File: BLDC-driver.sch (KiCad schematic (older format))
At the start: 109 parts, among them J1 PROG/DBG, J2 DBG, J3 RS485, J4 Encoder, J5 Conn_01x06, Q1 FDMS8018, Q2 FDMS8018, Q3 FDMS8018, Q4 FDMS8018, Q5 FDMS8018, Q6 FDMS8018, Q7 BC807, U1 NCP81155, U11 SN75176AD, U2 STM32L412CB, U4 NCP81155, U5 NCP81155, U6 MP2359, U7 MIC5504-3.3YM5, U8 NCS213RSQT2G, U9 NCS213RSQT2G, Y1 16MHz

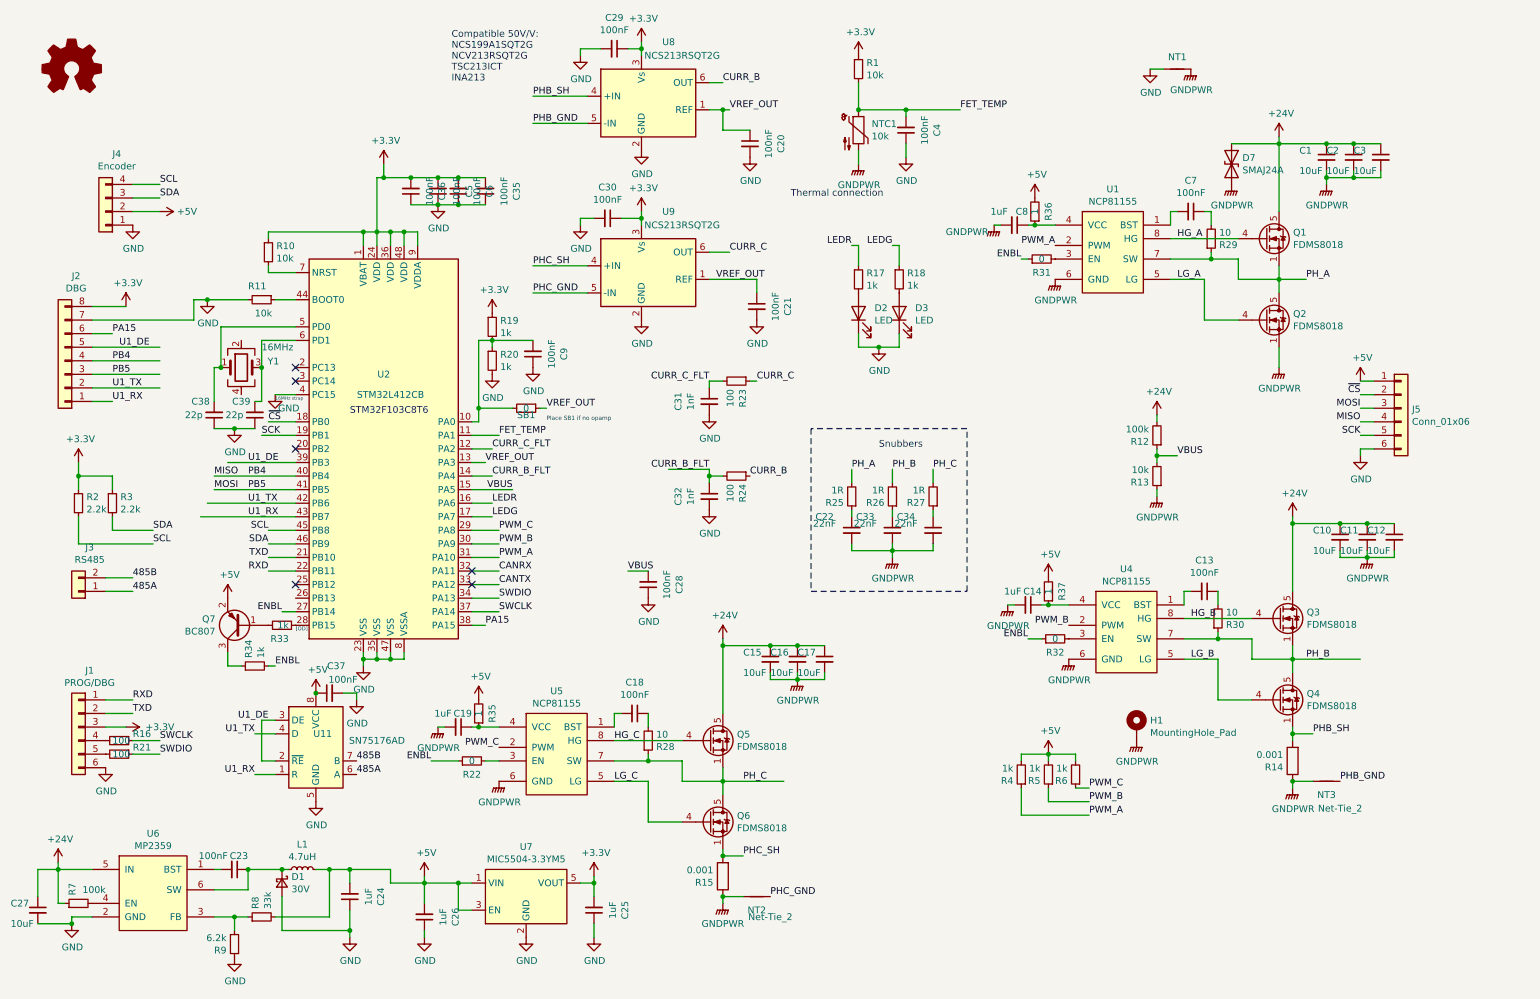
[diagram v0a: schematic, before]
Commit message: Update JLC BOM
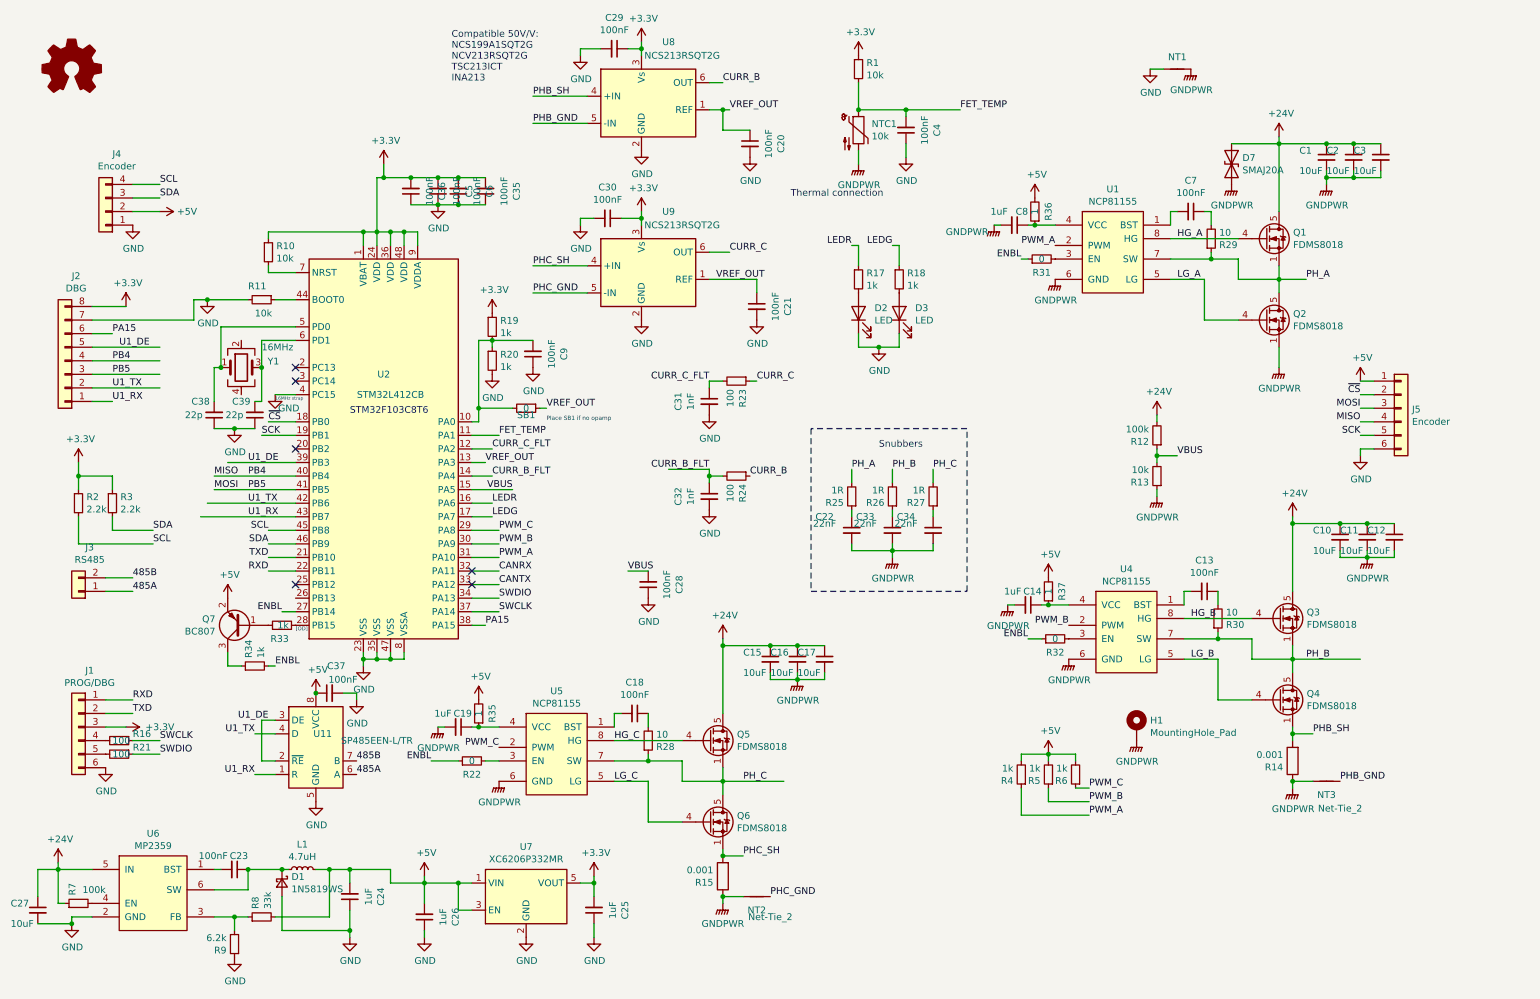
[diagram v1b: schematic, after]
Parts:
- C13, C18, C20, C21, C23, C28, C29, C30, C35, C36, C37, C4, C5, C6, C7, C9: Description [Basic] 100nF ±10% 16V X7R 0402 Multilayer Ceramic Capacito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 -> [Basic] X7R 100nF ±10% 16V 0402 Multilayer Ceramic Capacito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
- D1: value 30V -> 1N5819WS; Description (none) -> [Basic] 40V 1A 600mV @ 1A SOD-323 Schottky Barrier Diodes (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; JLCSMT (none) -> C191023; JLCSMT_PKG (none) -> SOD-323; MFR (none) -> Guangdong Hottech; MPN (none) -> 1N5819WS
- D2: Description LED, RED, 0603 -> [Basic] Red 615~630nm 1.9~2.2V 0603 Light Emitting Diodes (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; JLCSMT_PKG 0603 -> LED_0603
- D7: value SMAJ24A -> SMAJ20A; Description [Extended] Unidirectional 24V 26.7V 38.9V 10.3A SMA(DO-214A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 -> [Extended] Unidirectional 12.3A 32.4V 22.2V 20V SMA TVS ROHS; JLCSMT C10769 -> C353466; JLCSMT_PKG SMA,DO-214AC -> SMA; MFR RUILON(Shenzhen Ruilongyuan Elec) -> Shandong Jingdao Microelectronics; MPN SMAJ24A -> SMAJ20A
- J5: value Conn_01x06 -> Encoder; Description (none) -> [Extended] 6 0.020\"（0.50mm） 0.039\"（1.00mm） Forward Slip C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; JLCSMT_PKG (none) -> FPC-SMD; MFR (none) -> XFCN; MPN (none) -> F0502-B-06-10G-R
- R14, R15: Description [Extended] 0.001Ω ±1% 1W ±75ppm/℃ 1206 Current Sense Resist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 -> [Extended] ±75ppm/℃ ±1% 1W 0.001Ω 1206 Current Sense Resist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
- U1, U4, U5: Description (none) -> [Extended] DFN-8 Gate Drive ICs ROHS; JLCSMT (none) -> C173765; JLCSMT_PKG (none) -> DFN-8_EP_3.0x3.0x0.5P; MFR (none) -> ON Semiconductor; MPN NCP81151MNTBG -> NCP81155MNTXG
- U11: value SN75176AD -> SP485EEN-L/TR; Description [Basic] Transceiver RS485 1/1 SOIC-8_150mil RS-485/RS-422 I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 -> [Basic] Transceiver 1/1 RS485 10Mbps SOIC-8_150mil RS-485/R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; JLCSMT C7063 -> C6855; MFR Texas Instruments -> MaxLinear; MPN SN75176BDR -> SP485EEN-L/TR
- U2: Description (none) -> [Extended] 2.6V ~ 3.6V 32-Bit ARM? Cortex?-M3 108MHz FLASH 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; JLCSMT (none) -> C77994; JLCSMT_PKG (none) -> TQFP-48_7.0x7.0x0.5P; MFR (none) -> GigaDevice Semicon Beijing; MPN (none) -> GD32F103C8T6
- U7: value MIC5504-3.3YM5 -> XC6206P332MR; Description (none) -> [Basic] Low Dropout Regulators(LDO) Positive Fixed 680mV @ 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; JLCSMT (none) -> C5446; JLCSMT_PKG (none) -> SOT-23-3L; MFR (none) -> Torex Semicon; MPN (none) -> XC6206P332MR
- U8, U9: Description (none) -> [Extended] SC-70-6(SOT-363) Current-Sensing Amplifiers ROHS; JLCSMT (none) -> C129948; JLCSMT_PKG (none) -> SOT-363; MFR (none) -> Texas Instruments; MPN (none) -> INA213AIDCKT

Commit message: Update 3V3 LDO
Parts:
- U7: footprint Package_TO_SOT_SMD:SOT-23-5 -> Package_TO_SOT_SMD:SOT-23; symbol Regulator_Linear:MIC5504-3.3YM5 -> Regulator_Linear:XC6206PxxxMR
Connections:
- wire segments 337 -> 334
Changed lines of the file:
@@
 L power:GND #PWR046
 U 1 1 5EEF16F9
-P 4250 7350
-F 0 "#PWR046" H 4250 7100 50  0001 C CNN
-F 1 "GND" H 4255 7177 50  0000 C CNN
-F 2 "" H 4250 7350 50  0001 C CNN
-F 3 "" H 4250 7350 50  0001 C CNN
-	1    4250 7350
+P 4200 7250
+F 0 "#PWR046" H 4200 7000 50  0001 C CNN
+F 1 "GND" H 4205 7077 50  0000 C CNN
+F 2 "" H 4200 7250 50  0001 C CNN
+F 3 "" H 4200 7250 50  0001 C CNN
+	1    4200 7250
 	1    0    0    -1
 $EndComp
@@
 $EndComp
 $Comp
-L Regulator_Linear:MIC5504-3.3YM5 U7
+L Regulator_Linear:XC6206PxxxMR U7
 U 1 1 5EEEC834
-P 4250 7050
-F 0 "U7" H 4250 7417 50  0000 C CNN
-F 1 "XC6206P332MR" H 4250 7326 50  0000 C CNN
-F 2 "Package_TO_SOT_SMD:SOT-23-5" H 4250 6650 50  0001 C CNN
-F 3 "https://datasheet.lcsc.com/szlcsc/Torex-Semicon-XC6206P332MR_C5446.pdf" H 4000 7300 50  0001 C CNN
-F 4 "C5446" H 0   0   50  0001 C CNN "JLCSMT"
-F 5 "[Basic] Low Dropout Regulators(LDO) Positive Fixed 680mV @ 100mA 6V 3.3V 200mA SOT-23-3L RoHS" H 0   0   50  0001 C CNN "Description"
-F 6 "XC6206P332MR" H 0   0   50  0001 C CNN "MPN"
-F 7 "Torex Semicon" H 0   0   50  0001 C CNN "MFR"
-F 8 "SOT-23-3L" H 0   0   50  0001 C CNN "JLCSMT_PKG"
-	1    4250 7050
+P 4200 6950
+F 0 "U7" H 4200 7317 50  0000 C CNN
+F 1 "XC6206P332MR" H 4200 7226 50  0000 C CNN
+F 2 "Package_TO_SOT_SMD:SOT-23" H 4200 6550 50  0001 C CNN
+F 3 "https://datasheet.lcsc.com/szlcsc/Torex-Semicon-XC6206P332MR_C5446.pdf" H 3950 7200 50  0001 C CNN
+F 4 "C5446" H -50 -100 50  0001 C CNN "JLCSMT"
+F 5 "[Basic] Low Dropout Regulators(LDO) Positive Fixed 680mV @ 100mA 6V 3.3V 200mA SOT-23-3L RoHS" H -50 -100 50  0001 C CNN "Description"
+F 6 "XC6206P332MR" H -50 -100 50  0001 C CNN "MPN"
+F 7 "Torex Semicon" H -50 -100 50  0001 C CNN "MFR"
+F 8 "SOT-23-3L" H -50 -100 50  0001 C CNN "JLCSMT_PKG"
+	1    4200 6950
 	1    0    0    -1
 $EndComp
@@
 	1550 2000 1350 2000
 Wire Wire Line
-	3850 7150 3750 7150
-Wire Wire Line
-	3750 7150 3750 6950
-Wire Wire Line
-	3750 6950 3850 6950
-Wire Wire Line
 	3500 6900 3500 6950
 Wire Wire Line
-	3500 6950 3750 6950
-Wire Wire Line
 	3500 7100 3500 6950
 Wire Wire Line
 	3500 7350 3500 7300
 Wire Wire Line
-	4650 6950 4750 6950
-Wire Wire Line
 	4750 6950 4750 7050
 Wire Wire Line
@@
 Connection ~ 950  3950
 Connection ~ 6700 1250
-Connection ~ 3750 6950
 Connection ~ 3500 6950
 Connection ~ 4750 6950
@@
 	1    0    0    -1
 $EndComp
+Wire Wire Line
+	3500 6950 3900 6950
+Wire Wire Line
+	4500 6950 4750 6950
 $EndSCHEMATC

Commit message: Add DC-DC compatible notes
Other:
- note added: "Compatible:\nEUP3458\nME3116"
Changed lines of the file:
@@
 Wire Wire Line
 	4500 6950 4750 6950
+Text Notes 1250 7550 0    50   ~ 0
+Compatible:\nEUP3458\nME3116
 $EndSCHEMATC

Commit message: Add another alt
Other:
- note added: "Compatible:\nEUP3458\nME3116\nSSP9451"
- note removed: "Compatible:\nEUP3458\nME3116"
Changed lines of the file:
@@
 Wire Wire Line
 	4500 6950 4750 6950
-Text Notes 1250 7550 0    50   ~ 0
-Compatible:\nEUP3458\nME3116
+Text Notes 1250 7650 0    50   ~ 0
+Compatible:\nEUP3458\nME3116\nSSP9451
 $EndSCHEMATC

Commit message: Rev 4 update
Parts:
- added C40: 100uF, Capacitor_SMD:CP_Elec_8x6.5, symbol Device:CP_Small
- added J6: PWR, Connector_JST:JST_VH_B2PS-VH_1x02_P3.96mm_Horizontal, symbol Connector_Generic:Conn_01x02
- C1, C10, C11, C12, C15, C16, C17, C2, C27, C3: value 10uF -> 22uF; Description [Basic] 10uF ±10% 50V X5R 1206 Multilayer Ceramic Capacitor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 -> [Basic] 25V 22uF X5R ±10% 1206 Multilayer Ceramic Capacitor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; JLCSMT C13585 -> C12891; MPN CL31A106KBHNNNE -> CL31A226KAHNNNE
- C13, C18, C20, C21, C23, C28, C29, C30, C35, C36, C37, C4, C5, C6, C7, C9: Description [Basic] X7R 100nF ±10% 16V 0402 Multilayer Ceramic Capacito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 -> [Basic] 16V 100nF X7R ±10% 0402 Multilayer Ceramic Capacito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
- C14, C19, C24, C8: Description [Basic] 1uF ±10% 25V X5R 0402 Multilayer Ceramic Capacitors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 -> [Basic] 25V 1uF X5R ±10% 0402 Multilayer Ceramic Capacitors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
- C22, C33, C34: Description [Basic] Multilayer Ceramic Capacitors MLCC - SMD/SMT 22nF 5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 -> [Basic] 50V 22nF X7R ±10% 0402 Multilayer Ceramic Capacitor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; MFR Guangdong Fenghua Advanced Tech -> FH(Guangdong Fenghua Advanced Tech)
- C25, C26: Description [Basic] 1uF ±10% 50V X5R 0603 Multilayer Ceramic Capacitors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 -> [Basic] 50V 1uF X5R ±10% 0603 Multilayer Ceramic Capacitors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
- C31, C32: Description [Basic] 1nF ±10% 50V X7R 0402 Multilayer Ceramic Capacitors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 -> [Basic] 50V 1nF X7R ±10% 0402 Multilayer Ceramic Capacitors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
- C38, C39: Description [Basic] 22pF ±5% 50V C0G 0402 Multilayer Ceramic Capacitors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 -> [Basic] 50V 22pF C0G ±5% 0402 Multilayer Ceramic Capacitors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
- D1: Description [Basic] 40V 1A 600mV @ 1A SOD-323 Schottky Barrier Diodes (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 -> [Basic] 40V 600mV@1A 1A SOD-323 Schottky Barrier Diodes (SB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
- D2: Description [Basic] Red 615~630nm 1.9~2.2V 0603 Light Emitting Diodes (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 -> [Basic] 20mA 285mcd 3.3V 518nm Colorless transparence -40℃~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; JLCSMT C2286 -> C72043; MFR Hubei KENTO Elec -> Everlight Elec; MPN KT-0603R -> 19-217/GHC-YR1S2/3T
- D3: Description [Basic] Green 520~535nm 0603 Light Emitting Diodes (LED) Ro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 -> [Basic] 20mA 285mcd 3.3V 518nm Colorless transparence -40℃~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
- D7: Description [Extended] Unidirectional 12.3A 32.4V 22.2V 20V SMA TVS ROHS -> [Extended] 12.3A 32.4V 22.2V 20V Bi-Directional SMA(DO-214A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; JLCSMT C353466 -> C309871; MFR Shandong Jingdao Microelectronics -> Brightking Elec (TAIWAN); MPN SMAJ20A -> SMAJ20CA
- J5: value Encoder -> Encoder/SPI; footprint BLDC-Servo:FPC-SMD_F0502-B-06-10G-R -> JLC:FPC-SMD_F0502-B-06-10G-R; Description [Extended] 6 0.020\"（0.50mm） 0.039\"（1.00mm） Forward Slip C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 -> [Extended] Clamshell 6 Bottom Contact Surface Mount 0.5mm S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
- L1: Description [Extended] 4.7uH ±20% 1.3A 196mΩ SMD,3x3x1.2mm Power Induct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 -> [Extended] 1.3A 4.7uH ±20% 196mΩ SMD Power Inductors ROHS
- NTC1: Description Thermistor, NTC, 10 kohm, NCU Series, 3380 K, SMD, 0603 [16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 -> [Extended] 10kΩ -40℃~+125℃ 3455K 0.31mA 100mW 3334K ±1% 338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; JLCSMT_PKG RES-SMD -> 0603; MFR MURATA -> Murata Electronics; MPN NCU18XH103F60RB -> NCP18XH103F03RB
- Q7: Description [Basic] PNP 600mA 150V 300mW SOT-23(SOT-23-3) Bipolar Trans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 -> [Basic] 150V 300mW 600mA 200@10mA,5V 100MHz 500mV@50mA,5mA 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
- R1, R10, R11, R13: Description [Basic] 10kΩ ±1% 1/16W ±100ppm/℃ 0402 Chip Resistor - Surfa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 -> [Basic] ±1% 1/16W Thick Film Resistors 50V ±100ppm/℃ -55℃~+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
- R12, R7: Description [Basic] 100kΩ ±1% 1/16W ±100ppm/℃ 0402 Chip Resistor - Surf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 -> [Basic] ±1% 1/16W Thick Film Resistors 50V ±100ppm/℃ -55℃~+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
- R14, R15: Description [Extended] ±75ppm/℃ ±1% 1W 0.001Ω 1206 Current Sense Resist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 -> [Extended] 1W 0.001Ω ±75ppm/℃ ±1% 1206 Current Sense Resist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
- R16, R21, R23, R24: Description [Basic] 100Ω ±1% 1/16W ±200ppm/℃ 0402 Chip Resistor - Surfa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 -> [Basic] ±1% 1/16W Thick Film Resistors 50V ±200ppm/℃ -55℃~+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
- R17, R18: Description [Basic] 1kΩ ±1% 0.1W ±100ppm/℃ 0603 Chip Resistor - Surface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 -> [Basic] ±1% 1/10W Thick Film Resistors 75V ±100ppm/℃ -55℃~+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
- R19, R20, R33, R34, R4, R5, R6: Description [Basic] 1kΩ ±1% 1/16W ±100ppm/℃ 0402 Chip Resistor - Surfac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 -> [Basic] ±1% 1/16W Thick Film Resistors 50V ±100ppm/℃ -55℃~+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
- R2, R3: Description [Basic] Chip Resistor - Surface Mount 2.2KOhms ±1% 1/10W 06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 -> [Basic] ±1% 1/10W Thick Film Resistors 75V ±100ppm/℃ -55℃~+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; MFR Uniroyal Elec -> UNI-ROYAL(Uniroyal Elec)
- R22, R31, R32: Description [Basic] 0Ω ±1% 0.1W 0603 Chip Resistor - Surface Mount RoHS -> [Basic] ±1% 1/10W Thick Film Resistors 75V -55℃~+155℃ 0Ω 06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
- R25, R26, R27, R35, R36, R37: Description [Basic] 1Ω ±1% 1/16W ±400ppm/℃ 0402 Chip Resistor - Surface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 -> [Basic] ±1% 1/16W Thick Film Resistors 50V ±200ppm/℃ -55℃~+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
- R28, R29, R30: Description [Basic] Chip Resistor - Surface Mount 10Ohms ±1% 1/16W 0402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 -> [Basic] ±1% 1/16W Thick Film Resistors 50V ±200ppm/℃ -55℃~+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; MFR Uniroyal Elec -> UNI-ROYAL(Uniroyal Elec)
- R8: Description [Basic] 33kΩ ±1% 0.1W ±100ppm/℃ 0603 Chip Resistor - Surfac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 -> [Basic] ±1% 1/10W Thick Film Resistors 75V ±100ppm/℃ -55℃~+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
- R9: Description [Basic] 6.2kΩ ±1% 0.1W ±100ppm/℃ 0603 Chip Resistor - Surfa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 -> [Basic] ±1% 1/10W Thick Film Resistors 75V ±100ppm/℃ -55℃~+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
- SB1: Description [Basic] 0Ω ±1% 1/16W ±800ppm/℃ 0402 Chip Resistor - Surface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 -> [Basic] ±1% 1/16W Thick Film Resistors 50V ±800ppm/℃ -55℃~+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
- U1, U4, U5: MFR ON Semiconductor -> onsemi
- U11: Description [Basic] Transceiver 1/1 RS485 10Mbps SOIC-8_150mil RS-485/R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 -> [Basic] 10Mbps RS485 Transceiver SOIC-8_150mil RS-485/RS-42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
- U2: value STM32L412CB -> GD32F330C8T6; Description [Extended] 2.6V ~ 3.6V 32-Bit ARM? Cortex?-M3 108MHz FLASH 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 -> [Extended] 64KB -40℃~+85℃ 2.6V~3.6V ARM Cortex-M4 1@x16bit 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; JLCSMT C77994 -> C129291; JLCSMT_PKG TQFP-48_7.0x7.0x0.5P -> LQFP-48_7.0x7.0x0.5P; MPN GD32F103C8T6 -> GD32F330C8T6
- U7: Description [Basic] Low Dropout Regulators(LDO) Positive Fixed 680mV @ 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 -> [Basic] 200mA 680mV@(100mA) Fixed 3.3V~3.3V Positive 1 6V S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
- U8, U9: JLCSMT C129948 -> C59135; MPN INA213AIDCKT -> INA199A1DCKR
- Y1: Description [Basic] SMD Crystal Resonators 16MHz ±10ppm SMD-3225_4P RoHS -> [Basic] 16MHz SMD Crystal Resonator 9pF ±10ppm ±30ppm -40℃~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
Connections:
- wire segments 334 -> 336
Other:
- note added: "Compatible 50V/V:\nNCS199A1SQT2G\nNCV213RSQT2G\nTSC213ICT\nINA213\nWS74199x1\nTP213"
- note removed: "Compatible 50V/V:\nNCS199A1SQT2G\nNCV213RSQT2G\nTSC213ICT\nINA213"

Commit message: Latest revision
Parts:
- removed J5: Encoder/SPI, JLC:FPC-SMD_F0502-B-06-10G-R, symbol Connector_Generic:Conn_01x06
- added J5, J7: Conn_01x04, Connector_PinHeader_2.00mm:PinHeader_1x04_P2.00mm_Vertical, symbol Connector_Generic:Conn_01x04
- C40, Q7, U7, U8, U9: JLCPCB_CORRECTION (none) -> 0;0;180
- H1, J1, J2, J3, J6, NT1, NT2, NT3: JLCPCB_IGNORE (none) -> 1
- Q1, Q2, Q3, Q4, Q5, Q6: footprint Package_TO_SOT_SMD:TDSON-8-1 -> JLC:FDMS8018; JLCPCB_IGNORE (none) -> 1
- U1, U4, U5: symbol BLDC-driver-rescue:NCP81151-userdvc -> BLDC-driver:NCP81151-userdvc
- U11, U2: JLCPCB_CORRECTION (none) -> 0;0;-90
- U6: symbol BLDC-driver-rescue:MP2359 -> BLDC-driver:MP2359; JLCPCB_CORRECTION (none) -> 0;0;-180
- Y1: JLCPCB_CORRECTION (none) -> 0;0;-180
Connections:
- wire segments 336 -> 340

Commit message: Rev 4
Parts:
- added H2, H3: MountingHole_Pad, MountingHole:MountingHole_3.2mm_M3_DIN965_Pad_TopOnly, symbol Mechanical:MountingHole_Pad
- H1: footprint MountingHole:MountingHole_3.2mm_M3_DIN965_Pad -> MountingHole:MountingHole_3.2mm_M3_DIN965_Pad_TopOnly
- J4, J5, J7: JLCPCB_IGNORE (none) -> 1
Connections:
- net labels added: SPI0_MISO, SPI0_MOSI, SPI0_NSS, SPI0_SCK
- net labels removed: MISO, MOSI, PA15, PB4, PB5, SCK, ~CS
- wire segments 340 -> 341
- no-connect marks 6 -> 3
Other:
- note added: "rev4 strap"
- moved on the sheet: J5
